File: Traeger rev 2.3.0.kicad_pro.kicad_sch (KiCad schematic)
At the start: 43 parts, among them J1 MAX6675, J10 Buttons, J2 Time of Flight Sensor, J3 MAX31865-RTD, J5 Rotary Encoder, J6 ADS1115 0x49, J7 Temp Sensors, J8 Temp Sensors, J9 Conn_01x06_Socket, K1 Fan SSR - OMRON G3MC-202PL, K3 Auger SSR - OMRON G3MC-202PL, K6 Igniter SSR - OMRON G3MC-202PL, Q1 BC547, Q2 BC547, Q6 BC547, U1 ESP32-S3-DevKitC

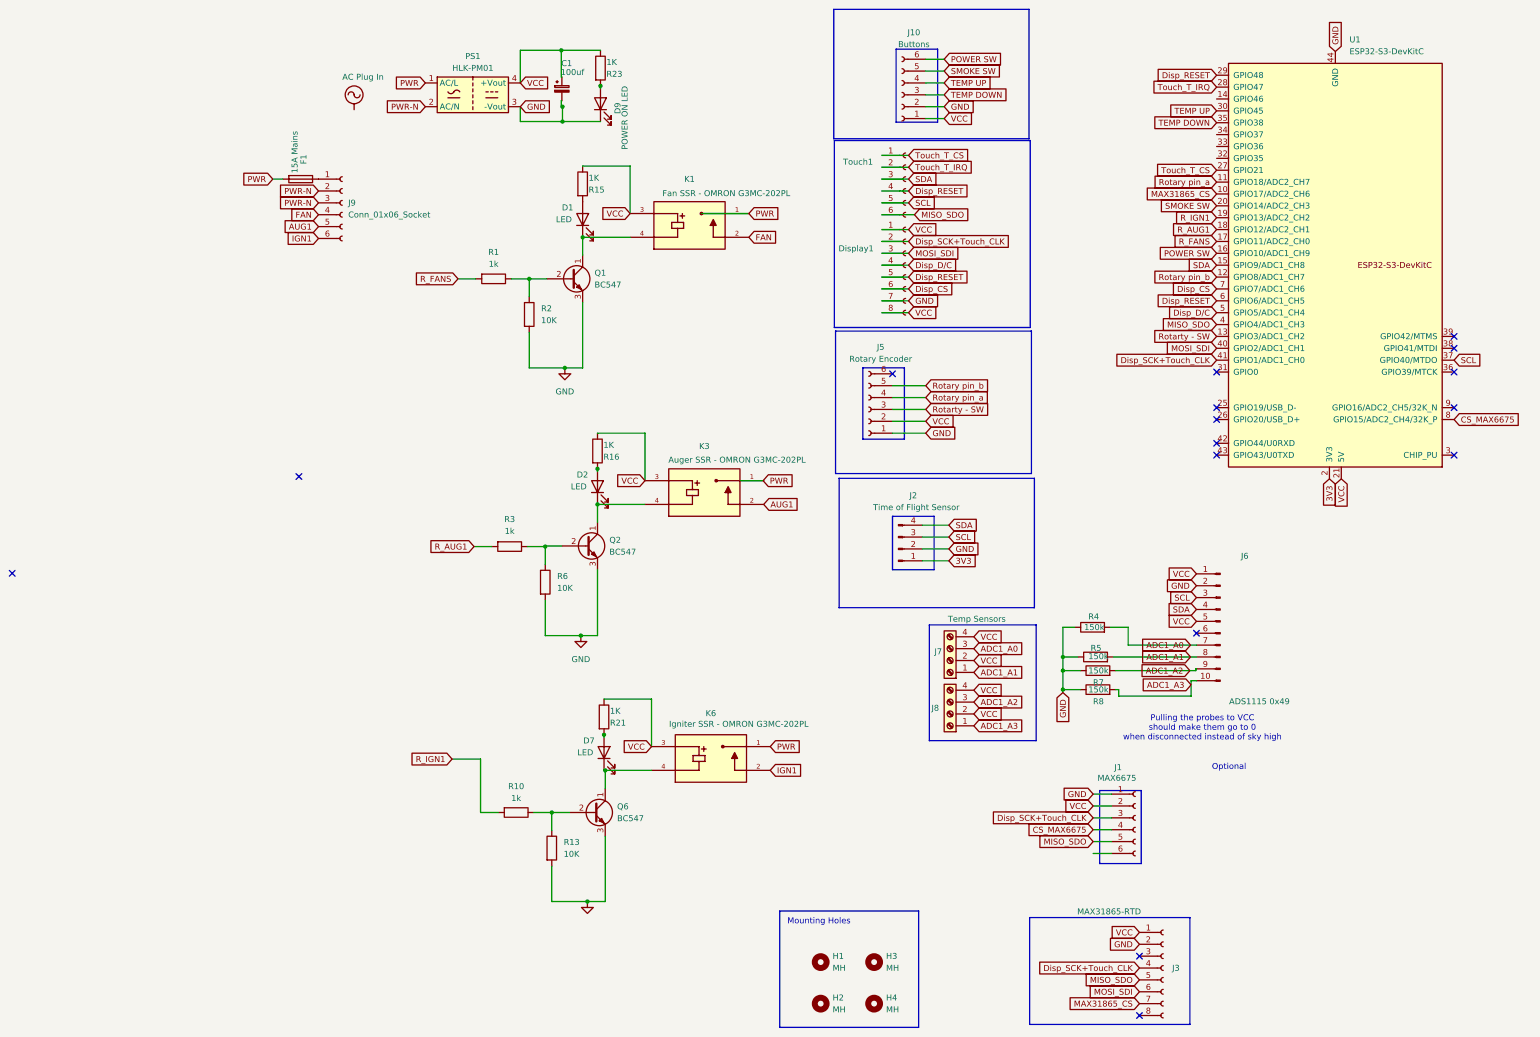
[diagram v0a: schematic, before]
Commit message: Update KiCad schematic and PCB for hardware changes
- ADS1115 VCC moved from 5V to 3.3V rail
- Pull-down resistors R_A0/R_A1 changed from 150kΩ to 1kΩ

Co-Authored-By: Claude Sonnet 4.6 <noreply@anthropic.com>
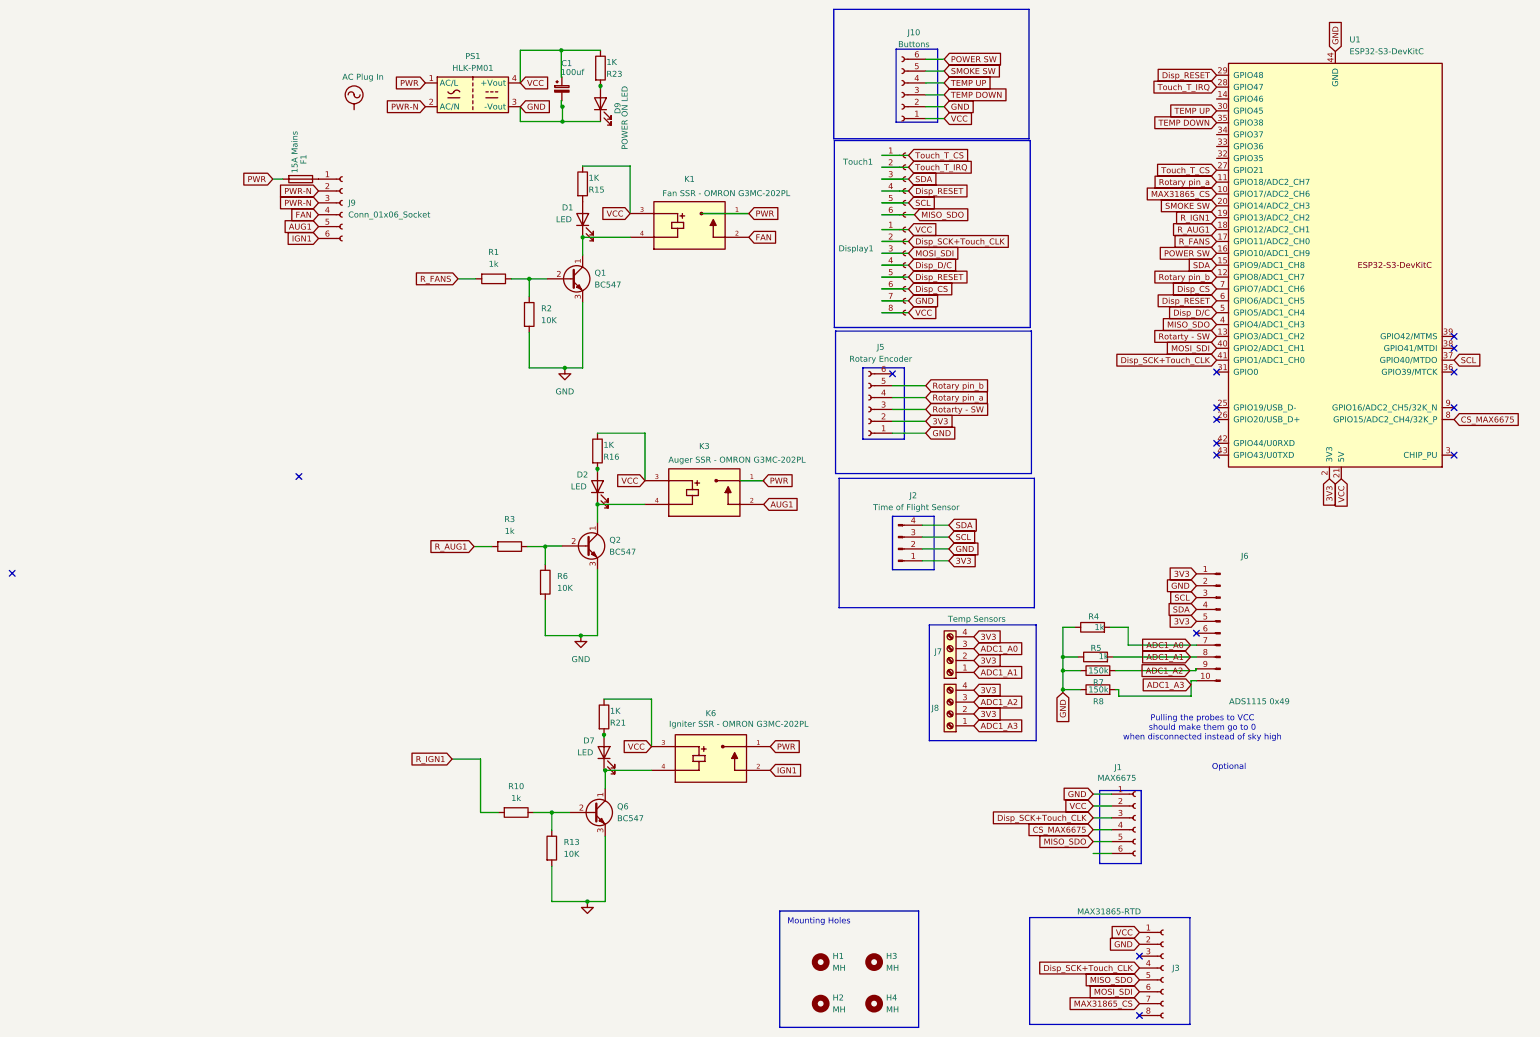
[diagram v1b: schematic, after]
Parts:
- R4, R5: value 150k -> 1k
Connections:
- net 3V3: now also J5.2 (Pin_2), J6.1 (Pin_1), J6.5 (Pin_5), J7.2 (Pin_2), J7.4 (Pin_4), J8.2 (Pin_2), J8.4 (Pin_4)
- net VCC: no longer J5.2 (Pin_2), J6.1 (Pin_1), J6.5 (Pin_5), J7.2 (Pin_2), J7.4 (Pin_4), J8.2 (Pin_2), J8.4 (Pin_4)
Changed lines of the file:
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@@
 (kicad_sch
-	(version 20231120)
+	(version 20250114)
 	(generator "eeschema")
-	(generator_version "8.0")
+	(generator_version "9.0")
 	(paper "A3")
 	(title_block
@@
 		(comment 3 "1.01 - updated display conns")
 	)
+	(rectangle
+		(start 180.594 116.078)
+		(end 222.377 143.764)
+		(stroke
+			(width 0)
+			(type default)
+		)
+		(fill
+			(type none)
+		)
+	)
+	(rectangle
+		(start 192.786 24.257)
+		(end 201.676 39.878)
+		(stroke
+			(width 0)
+			(type default)
+		)
+		(fill
+			(type none)
+		)
+	)
+	(rectangle
+		(start 167.894 208.661)
+		(end 197.612 233.553)
+		(stroke
+			(width 0)
+			(type default)
+		)
+		(fill
+			(type none)
+		)
+	)
+	(rectangle
+		(start 185.674 92.456)
+		(end 194.564 107.696)
+		(stroke
+			(width 0)
+			(type default)
+		)
+		(fill
+			(type none)
+		)
+	)
+	(rectangle
+		(start 179.832 84.582)
+		(end 221.742 115.062)
+		(stroke
+			(width 0)
+			(type default)
+		)
+		(fill
+			(type none)
+		)
+	)
+	(rectangle
+		(start 199.898 147.447)
+		(end 222.758 172.212)
+		(stroke
+			(width 0)
+			(type default)
+		)
+		(fill
+			(type none)
+		)
+	)
+	(rectangle
+		(start 245.237 198.501)
+		(end 236.347 182.88)
+		(stroke
+			(width 0)
+			(type default)
+		)
+		(fill
+			(type none)
+		)
+	)
+	(rectangle
+		(start 221.361 210.058)
+		(end 255.651 232.918)
+		(stroke
+			(width 0)
+			(type default)
+		)
+		(fill
+			(type none)
+		)
+	)
+	(rectangle
+		(start 192.024 124.206)
+		(end 200.914 135.636)
+		(stroke
+			(width 0)
+			(type default)
+		)
+		(fill
+			(type none)
+		)
+	)
+	(rectangle
+		(start 179.578 43.815)
+		(end 221.488 83.82)
+		(stroke
+			(width 0)
+			(type default)
+		)
+		(fill
+			(type none)
+		)
+	)
+	(rectangle
+		(start 179.451 15.748)
+		(end 221.234 43.434)
+		(stroke
+			(width 0)
+			(type default)
+		)
+		(fill
+			(type none)
+		)
+	)
+	(text "Pulling the probes to VCC \nshould make them go to 0 \nwhen disconnected instead of sky high"
+		(exclude_from_sim no)
+		(at 258.318 169.545 0)
+		(effects
+			(font
+				(size 1.27 1.27)
+			)
+		)
+	)
+	(text "Optional"
+		(exclude_from_sim no)
+		(at 264.033 177.927 0)
+		(effects
+			(font
+				(size 1.27 1.27)
+			)
+		)
+	)
+	(text "Mounting Holes"
+		(exclude_from_sim no)
+		(at 176.276 210.947 0)
+		(effects
+			(font
+				(size 1.27 1.27)
+			)
+		)
+	)
 	(junction
 		(at 125.349 149.733)
@@
 		)
 	)
-	(rectangle
-		(start 180.594 116.078)
-		(end 222.377 143.764)
-		(stroke
-			(width 0)
-			(type default)
-		)
-		(fill
-			(type none)
-		)
-	)
-	(rectangle
-		(start 192.786 24.257)
-		(end 201.676 39.878)
-		(stroke
-			(width 0)
-			(type default)
-		)
-		(fill
-			(type none)
-		)
-	)
-	(rectangle
-		(start 167.894 208.661)
-		(end 197.612 233.553)
-		(stroke
-			(width 0)
-			(type default)
-		)
-		(fill
-			(type none)
-		)
-	)
-	(rectangle
-		(start 185.674 92.456)
-		(end 194.564 107.696)
-		(stroke
-			(width 0)
-			(type default)
-		)
-		(fill
-			(type none)
-		)
-	)
-	(rectangle
-		(start 179.832 84.582)
-		(end 221.742 115.062)
-		(stroke
-			(width 0)
-			(type default)
-		)
-		(fill
-			(type none)
-		)
-	)
-	(rectangle
-		(start 199.898 147.447)
-		(end 222.758 172.212)
-		(stroke
-			(width 0)
-			(type default)
-		)
-		(fill
-			(type none)
-		)
-	)
-	(rectangle
-		(start 245.237 198.501)
-		(end 236.347 182.88)
-		(stroke
-			(width 0)
-			(type default)
-		)
-		(fill
-			(type none)
-		)
-	)
-	(rectangle
-		(start 221.361 210.058)
-		(end 255.651 232.918)
-		(stroke
-			(width 0)
-			(type default)
-		)
-		(fill
-			(type none)
-		)
-	)
-	(rectangle
-		(start 192.024 124.206)
-		(end 200.914 135.636)
-		(stroke
-			(width 0)
-			(type default)
-		)
-		(fill
-			(type none)
-		)
-	)
-	(rectangle
-		(start 179.578 43.815)
-		(end 221.488 83.82)
-		(stroke
-			(width 0)
-			(type default)
-		)
-		(fill
-			(type none)
-		)
-	)
-	(rectangle
-		(start 179.451 15.748)
-		(end 221.234 43.434)
-		(stroke
-			(width 0)
-			(type default)
-		)
-		(fill
-			(type none)
-		)
-	)
 	(image
 		(at 271.018 147.32)
@@
 		)
 	)
-	(text "Pulling the probes to VCC \nshould make them go to 0 \nwhen disconnected instead of sky high"
-		(exclude_from_sim no)
-		(at 258.318 169.545 0)
-		(effects
-			(font
-				(size 1.27 1.27)
-			)
-		)
-	)
-	(text "Optional"
-		(exclude_from_sim no)
-		(at 264.033 177.927 0)
-		(effects
-			(font
-				(size 1.27 1.27)
-			)
-		)
-	)
-	(text "Mounting Holes"
-		(exclude_from_sim no)
-		(at 176.276 210.947 0)
-		(effects
-			(font
-				(size 1.27 1.27)
-			)
-		)
-	)
 	(global_label "SCL"
 		(shape input)
@@
 		)
 	)
-	(global_label "VCC"
+	(global_label "3V3"
 		(shape input)
 		(at 199.136 103.886 0)
@@
 		)
 		(property "Intersheetrefs" "${INTERSHEET_REFS}"
-			(at 205.7498 103.886 0)
+			(at 205.6288 103.886 0)
 			(effects
 				(font
@@
 		)
 	)
-	(global_label "VCC"
+	(global_label "3V3"
 		(shape input)
 		(at 257.048 146.685 180)
@@
 		)
 		(property "Intersheetrefs" "${INTERSHEET_REFS}"
-			(at 250.4342 146.685 0)
+			(at 250.5552 146.685 0)
 			(effects
 				(font
@@
 		)
 	)
-	(global_label "VCC"
+	(global_label "3V3"
 		(shape input)
 		(at 209.423 161.417 0)
@@
 		)
 		(property "Intersheetrefs" "${INTERSHEET_REFS}"
-			(at 216.0368 161.417 0)
+			(at 215.9158 161.417 0)
 			(effects
 				(font
@@
 		)
 	)
-	(global_label "VCC"
+	(global_label "3V3"
 		(shape input)
 		(at 209.423 149.987 0)
@@
 		)
 		(property "Intersheetrefs" "${INTERSHEET_REFS}"
-			(at 216.0368 149.987 0)
+			(at 215.9158 149.987 0)
 			(effects
 				(font
@@
 		)
 	)
-	(global_label "VCC"
+	(global_label "3V3"
 		(shape input)
 		(at 257.048 136.525 180)
@@
 		)
 		(property "Intersheetrefs" "${INTERSHEET_REFS}"
-			(at 250.4342 136.525 0)
+			(at 250.5552 136.525 0)
 			(effects
 				(font
@@
 		)
 	)
-	(global_label "VCC"
+	(global_label "3V3"
 		(shape input)
 		(at 209.423 166.497 0)
@@
 		)
 		(property "Intersheetrefs" "${INTERSHEET_REFS}"
-			(at 216.0368 166.497 0)
+			(at 215.9158 166.497 0)
 			(effects
 				(font
@@
 		)
 	)
-	(global_label "VCC"
+	(global_label "3V3"
 		(shape input)
 		(at 209.423 155.067 0)
@@
 		)
 		(property "Intersheetrefs" "${INTERSHEET_REFS}"
-			(at 216.0368 155.067 0)
+			(at 215.9158 155.067 0)
 			(effects
 				(font
@@
 			)
 		)
-		(property "Value" "150k"
+		(property "Value" "1k"
 			(at 237.363 147.955 90)
 			(effects
@@
 			)
 		)
-		(property "Value" "150k"
+		(property "Value" "1k"
 			(at 238.252 154.178 90)
 			(effects
@@
 		)
 	)
+	(embedded_fonts no)
 )
